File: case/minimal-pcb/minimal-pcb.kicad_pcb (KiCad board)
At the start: 2 copper layers, 70 x 70 mm, 10 parts, among them J1 USB_C_Receptacle_USB2.0

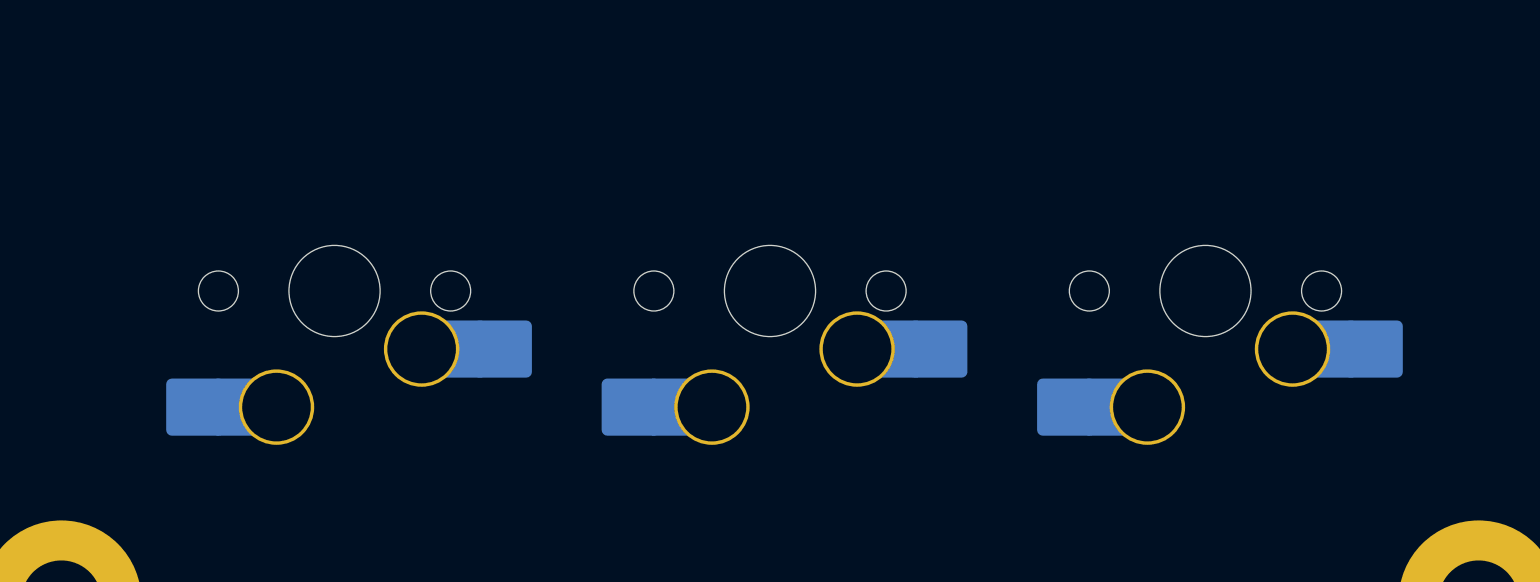
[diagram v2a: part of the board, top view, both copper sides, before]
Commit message: fix: use south facing switches in minimal PCB
didn't notice until I saw the positioning of the hotswap sockets on the minoripad PCB...
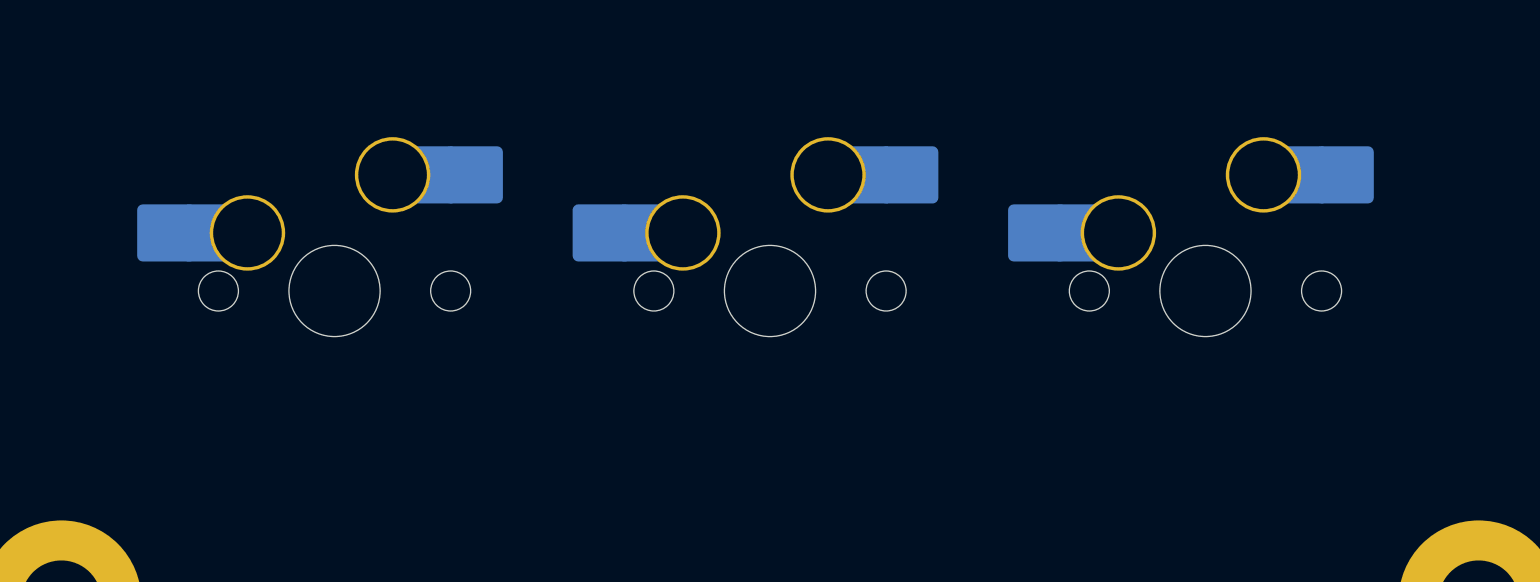
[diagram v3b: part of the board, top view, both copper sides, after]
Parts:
- turned MX1 to 180 degrees
- turned MX2 to 180 degrees
- turned MX3 to 180 degrees
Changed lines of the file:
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@@
   (net 25 "unconnected-(D2-DIN-Pad4)")
   (footprint "PCM_marbastlib-mx:SW_MX_HS_1u" (layer "B.Cu")
-    (at 57.15 74.224147)
+    (at 57.15 74.224147 180)
     (descr "Footprint for Cherry MX style switches with Kailh hotswap socket")
     (property "Sheetfile" "minimal-pcb.kicad_sch")
@@
     (fp_arc (start 6.085176 4.75022) (mid 5.499389 6.164432) (end 4.085176 6.75022)
       (stroke (width 0.05) (type solid)) (layer "B.Fab"))
-    (pad "" np_thru_hole circle (at -5.08 0) (size 1.75 1.75) (drill 1.75) (layers "*.Cu" "*.Mask"))
-    (pad "" np_thru_hole circle (at 0 0) (size 3.9878 3.9878) (drill 3.9878) (layers "*.Cu" "*.Mask"))
-    (pad "" np_thru_hole circle (at 5.08 0) (size 1.75 1.75) (drill 1.75) (layers "*.Cu" "*.Mask"))
-    (pad "1" thru_hole circle (at 3.81 2.54) (size 3.3 3.3) (drill 3) (layers "*.Cu" "*.Mask")
+    (pad "" np_thru_hole circle (at -5.08 0 180) (size 1.75 1.75) (drill 1.75) (layers "*.Cu" "*.Mask"))
+    (pad "" np_thru_hole circle (at 0 0 180) (size 3.9878 3.9878) (drill 3.9878) (layers "*.Cu" "*.Mask"))
+    (pad "" np_thru_hole circle (at 5.08 0 180) (size 1.75 1.75) (drill 1.75) (layers "*.Cu" "*.Mask"))
+    (pad "1" thru_hole circle (at 3.81 2.54 180) (size 3.3 3.3) (drill 3) (layers "*.Cu" "*.Mask")
       (net 5 "unconnected-(MX3-Pad1)") (pinfunction "1") (pintype "passive"))
-    (pad "1" smd rect (at 5.635 2.54 180) (size 1.65 2.5) (layers "B.Cu")
+    (pad "1" smd rect (at 5.635 2.54) (size 1.65 2.5) (layers "B.Cu")
       (net 5 "unconnected-(MX3-Pad1)") (pinfunction "1") (pintype "passive"))
-    (pad "1" smd roundrect (at 7.36 2.54) (size 2.55 2.5) (layers "B.Cu" "B.Paste" "B.Mask") (roundrect_rratio 0.1)
+    (pad "1" smd roundrect (at 7.36 2.54 180) (size 2.55 2.5) (layers "B.Cu" "B.Paste" "B.Mask") (roundrect_rratio 0.1)
       (net 5 "unconnected-(MX3-Pad1)") (pinfunction "1") (pintype "passive"))
-    (pad "2" smd roundrect (at -6.09 5.08) (size 2.55 2.5) (layers "B.Cu" "B.Paste" "B.Mask") (roundrect_rratio 0.1)
+    (pad "2" smd roundrect (at -6.09 5.08 180) (size 2.55 2.5) (layers "B.Cu" "B.Paste" "B.Mask") (roundrect_rratio 0.1)
       (net 6 "unconnected-(MX3-Pad2)") (pinfunction "2") (pintype "passive"))
-    (pad "2" smd rect (at -4.34 5.08) (size 1.65 2.5) (layers "B.Cu")
+    (pad "2" smd rect (at -4.34 5.08 180) (size 1.65 2.5) (layers "B.Cu")
       (net 6 "unconnected-(MX3-Pad2)") (pinfunction "2") (pintype "passive"))
-    (pad "2" thru_hole circle (at -2.54 5.08) (size 3.3 3.3) (drill 3) (layers "*.Cu" "*.Mask")
+    (pad "2" thru_hole circle (at -2.54 5.08 180) (size 3.3 3.3) (drill 3) (layers "*.Cu" "*.Mask")
       (net 6 "unconnected-(MX3-Pad2)") (pinfunction "2") (pintype "passive"))
     (model "${KICAD7_3RD_PARTY}/3dmodels/com_github_ebastler_marbastlib/HS_Kailh_MX.step"
@@
   )
   (footprint "PCM_marbastlib-mx:SW_MX_HS_1u" (layer "B.Cu")
-    (at 76.2 74.224147)
+    (at 76.2 74.224147 180)
     (descr "Footprint for Cherry MX style switches with Kailh hotswap socket")
     (property "Sheetfile" "minimal-pcb.kicad_sch")
@@
     (fp_arc (start 6.085176 4.75022) (mid 5.499389 6.164432) (end 4.085176 6.75022)
       (stroke (width 0.05) (type solid)) (layer "B.Fab"))
-    (pad "" np_thru_hole circle (at -5.08 0) (size 1.75 1.75) (drill 1.75) (layers "*.Cu" "*.Mask"))
-    (pad "" np_thru_hole circle (at 0 0) (size 3.9878 3.9878) (drill 3.9878) (layers "*.Cu" "*.Mask"))
-    (pad "" np_thru_hole circle (at 5.08 0) (size 1.75 1.75) (drill 1.75) (layers "*.Cu" "*.Mask"))
-    (pad "1" thru_hole circle (at 3.81 2.54) (size 3.3 3.3) (drill 3) (layers "*.Cu" "*.Mask")
+    (pad "" np_thru_hole circle (at -5.08 0 180) (size 1.75 1.75) (drill 1.75) (layers "*.Cu" "*.Mask"))
+    (pad "" np_thru_hole circle (at 0 0 180) (size 3.9878 3.9878) (drill 3.9878) (layers "*.Cu" "*.Mask"))
+    (pad "" np_thru_hole circle (at 5.08 0 180) (size 1.75 1.75) (drill 1.75) (layers "*.Cu" "*.Mask"))
+    (pad "1" thru_hole circle (at 3.81 2.54 180) (size 3.3 3.3) (drill 3) (layers "*.Cu" "*.Mask")
       (net 3 "unconnected-(MX2-Pad1)") (pinfunction "1") (pintype "passive"))
-    (pad "1" smd rect (at 5.635 2.54 180) (size 1.65 2.5) (layers "B.Cu")
+    (pad "1" smd rect (at 5.635 2.54) (size 1.65 2.5) (layers "B.Cu")
       (net 3 "unconnected-(MX2-Pad1)") (pinfunction "1") (pintype "passive"))
-    (pad "1" smd roundrect (at 7.36 2.54) (size 2.55 2.5) (layers "B.Cu" "B.Paste" "B.Mask") (roundrect_rratio 0.1)
+    (pad "1" smd roundrect (at 7.36 2.54 180) (size 2.55 2.5) (layers "B.Cu" "B.Paste" "B.Mask") (roundrect_rratio 0.1)
       (net 3 "unconnected-(MX2-Pad1)") (pinfunction "1") (pintype "passive"))
-    (pad "2" smd roundrect (at -6.09 5.08) (size 2.55 2.5) (layers "B.Cu" "B.Paste" "B.Mask") (roundrect_rratio 0.1)
+    (pad "2" smd roundrect (at -6.09 5.08 180) (size 2.55 2.5) (layers "B.Cu" "B.Paste" "B.Mask") (roundrect_rratio 0.1)
       (net 4 "unconnected-(MX2-Pad2)") (pinfunction "2") (pintype "passive"))
-    (pad "2" smd rect (at -4.34 5.08) (size 1.65 2.5) (layers "B.Cu")
+    (pad "2" smd rect (at -4.34 5.08 180) (size 1.65 2.5) (layers "B.Cu")
       (net 4 "unconnected-(MX2-Pad2)") (pinfunction "2") (pintype "passive"))
-    (pad "2" thru_hole circle (at -2.54 5.08) (size 3.3 3.3) (drill 3) (layers "*.Cu" "*.Mask")
+    (pad "2" thru_hole circle (at -2.54 5.08 180) (size 3.3 3.3) (drill 3) (layers "*.Cu" "*.Mask")
       (net 4 "unconnected-(MX2-Pad2)") (pinfunction "2") (pintype "passive"))
     (model "${KICAD7_3RD_PARTY}/3dmodels/com_github_ebastler_marbastlib/HS_Kailh_MX.step"
@@
   )
   (footprint "PCM_marbastlib-mx:SW_MX_HS_1u" (layer "B.Cu")
-    (at 38.1 74.224147)
+    (at 38.1 74.224147 180)
     (descr "Footprint for Cherry MX style switches with Kailh hotswap socket")
     (property "Sheetfile" "minimal-pcb.kicad_sch")
@@
     (fp_arc (start 6.085176 4.75022) (mid 5.499389 6.164432) (end 4.085176 6.75022)
       (stroke (width 0.05) (type solid)) (layer "B.Fab"))
-    (pad "" np_thru_hole circle (at -5.08 0) (size 1.75 1.75) (drill 1.75) (layers "*.Cu" "*.Mask"))
-    (pad "" np_thru_hole circle (at 0 0) (size 3.9878 3.9878) (drill 3.9878) (layers "*.Cu" "*.Mask"))
-    (pad "" np_thru_hole circle (at 5.08 0) (size 1.75 1.75) (drill 1.75) (layers "*.Cu" "*.Mask"))
-    (pad "1" thru_hole circle (at 3.81 2.54) (size 3.3 3.3) (drill 3) (layers "*.Cu" "*.Mask")
+    (pad "" np_thru_hole circle (at -5.08 0 180) (size 1.75 1.75) (drill 1.75) (layers "*.Cu" "*.Mask"))
+    (pad "" np_thru_hole circle (at 0 0 180) (size 3.9878 3.9878) (drill 3.9878) (layers "*.Cu" "*.Mask"))
+    (pad "" np_thru_hole circle (at 5.08 0 180) (size 1.75 1.75) (drill 1.75) (layers "*.Cu" "*.Mask"))
+    (pad "1" thru_hole circle (at 3.81 2.54 180) (size 3.3 3.3) (drill 3) (layers "*.Cu" "*.Mask")
       (net 1 "unconnected-(MX1-Pad1)") (pinfunction "1") (pintype "passive"))
-    (pad "1" smd rect (at 5.635 2.54 180) (size 1.65 2.5) (layers "B.Cu")
+    (pad "1" smd rect (at 5.635 2.54) (size 1.65 2.5) (layers "B.Cu")
       (net 1 "unconnected-(MX1-Pad1)") (pinfunction "1") (pintype "passive"))
-    (pad "1" smd roundrect (at 7.36 2.54) (size 2.55 2.5) (layers "B.Cu" "B.Paste" "B.Mask") (roundrect_rratio 0.1)
+    (pad "1" smd roundrect (at 7.36 2.54 180) (size 2.55 2.5) (layers "B.Cu" "B.Paste" "B.Mask") (roundrect_rratio 0.1)
       (net 1 "unconnected-(MX1-Pad1)") (pinfunction "1") (pintype "passive"))
-    (pad "2" smd roundrect (at -6.09 5.08) (size 2.55 2.5) (layers "B.Cu" "B.Paste" "B.Mask") (roundrect_rratio 0.1)
+    (pad "2" smd roundrect (at -6.09 5.08 180) (size 2.55 2.5) (layers "B.Cu" "B.Paste" "B.Mask") (roundrect_rratio 0.1)
       (net 2 "unconnected-(MX1-Pad2)") (pinfunction "2") (pintype "passive"))
-    (pad "2" smd rect (at -4.34 5.08) (size 1.65 2.5) (layers "B.Cu")
+    (pad "2" smd rect (at -4.34 5.08 180) (size 1.65 2.5) (layers "B.Cu")
       (net 2 "unconnected-(MX1-Pad2)") (pinfunction "2") (pintype "passive"))
-    (pad "2" thru_hole circle (at -2.54 5.08) (size 3.3 3.3) (drill 3) (layers "*.Cu" "*.Mask")
+    (pad "2" thru_hole circle (at -2.54 5.08 180) (size 3.3 3.3) (drill 3) (layers "*.Cu" "*.Mask")
       (net 2 "unconnected-(MX1-Pad2)") (pinfunction "2") (pintype "passive"))
     (model "${KICAD7_3RD_PARTY}/3dmodels/com_github_ebastler_marbastlib/HS_Kailh_MX.step"

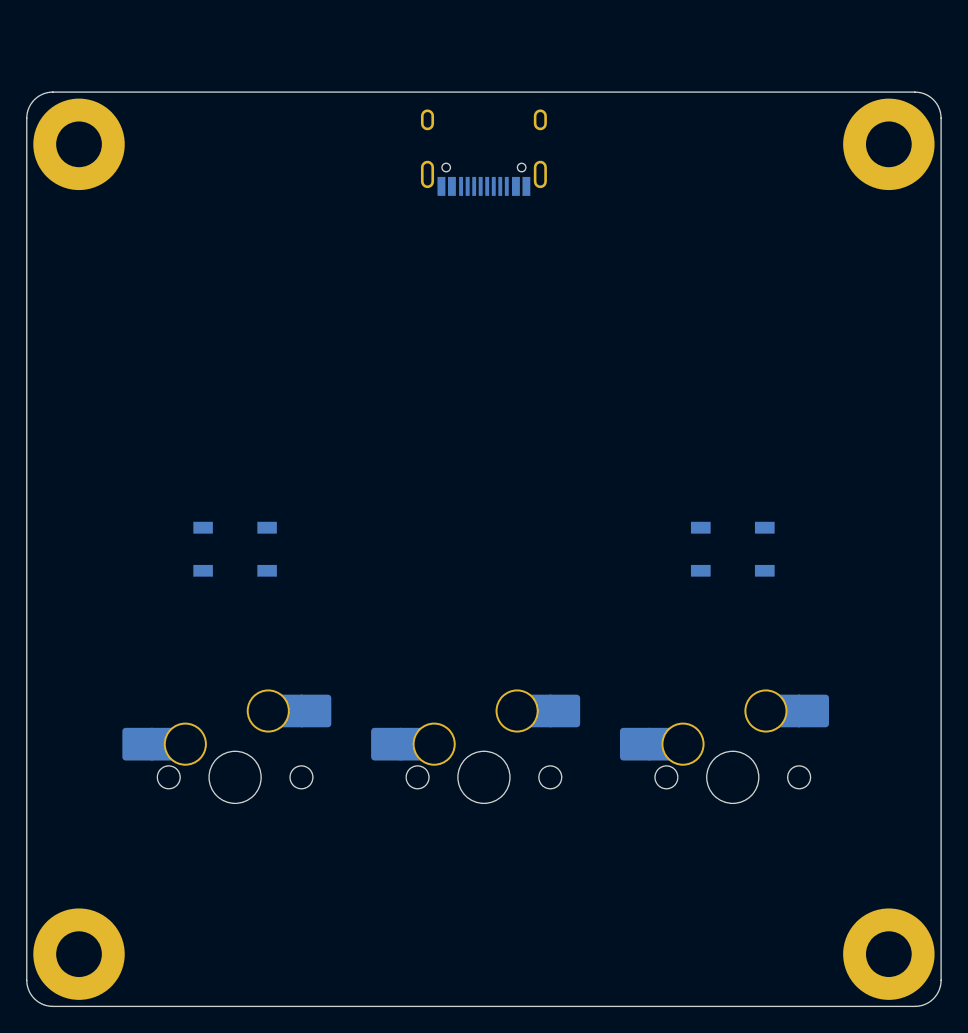
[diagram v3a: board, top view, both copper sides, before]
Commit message: chore: update minimal pcb
got the usb cutout dimensions wrong on the pcb... need to fix it
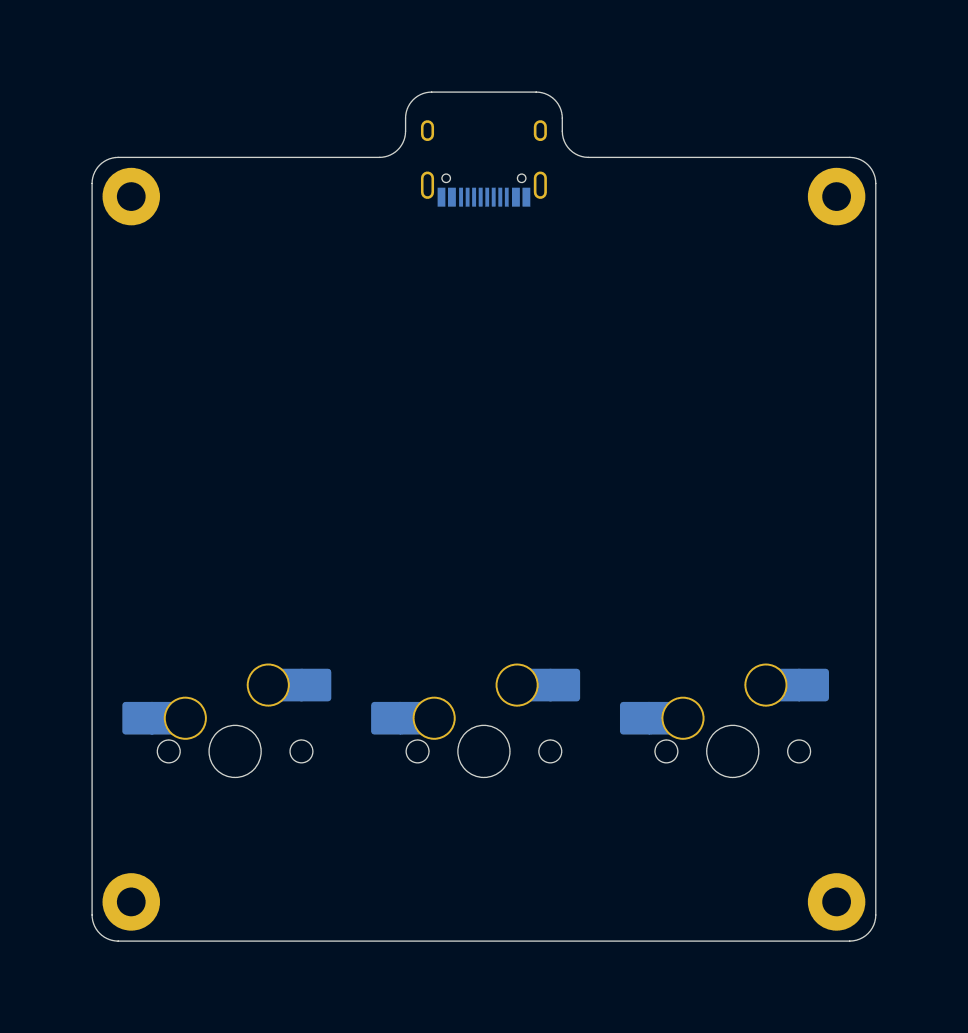
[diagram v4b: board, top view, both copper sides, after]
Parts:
- removed D1, D2: WS2812B, LED_SMD:LED_WS2812B_PLCC4_5.0x5.0mm_P3.2mm
- H1, H2, H3, H4: footprint MountingHole:MountingHole_3.5mm_Pad -> MountingHole:MountingHole_2.2mm_M2_Pad
- moved MX1 38.2 mm to (76.2, 72.2)
- moved MX3 19.2 mm to (38.1, 72.2)
- moved MX2 19.2 mm to (57.1, 72.2)
- moved H1 5.66 mm to (30.1, 29.8)
- moved H2 5.66 mm to (84.2, 29.8)
- moved H3 5.66 mm to (30.1, 83.8)
- moved H4 5.66 mm to (84.2, 83.8)
- moved J1 0.82 mm to (57.1, 25.8)
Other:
- board size 70 x 70 mm -> 60 x 65 mm
